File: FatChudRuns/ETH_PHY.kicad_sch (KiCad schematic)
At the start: 45 parts, among them U2 DP83848I

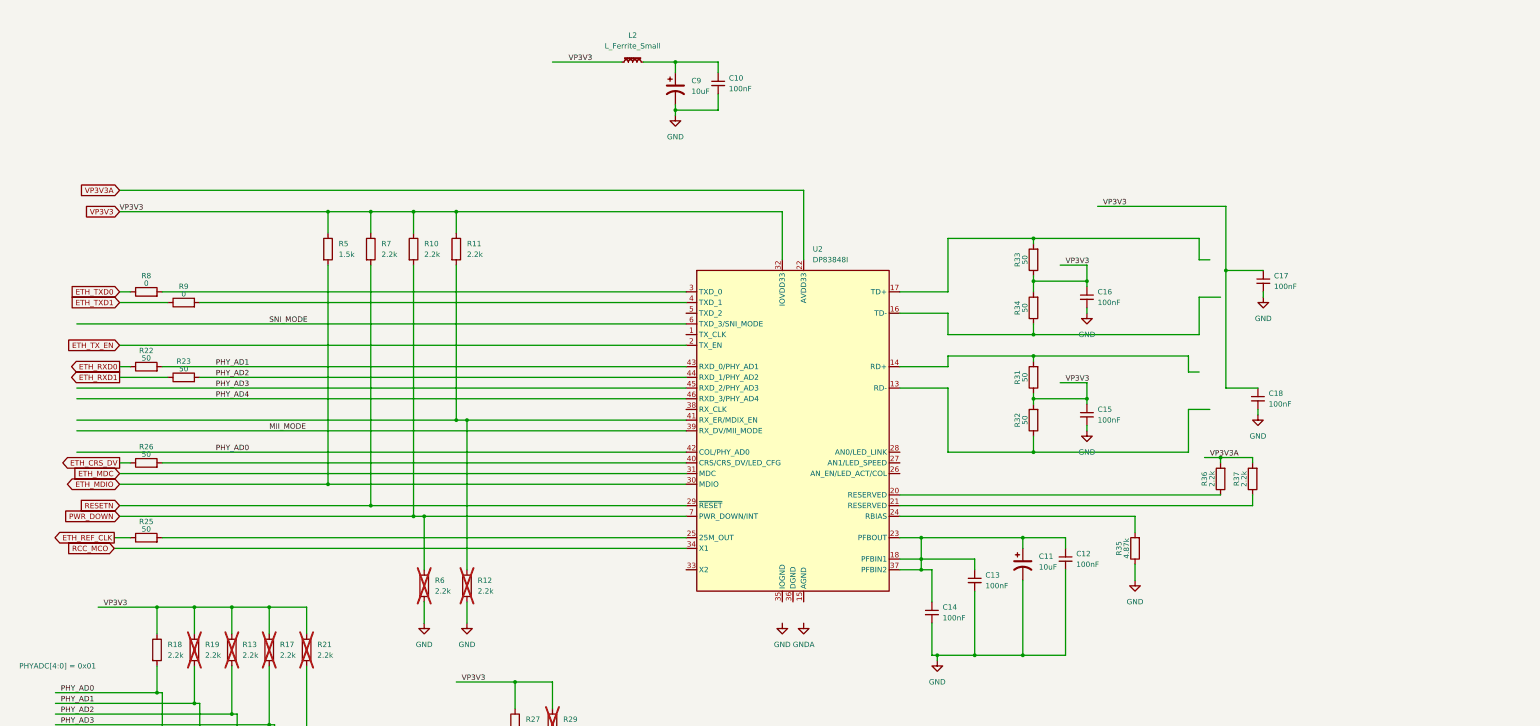
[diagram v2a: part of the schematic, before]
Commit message: selected rj45 w/ mag, fixed filtering for power, added snippets of layout recs
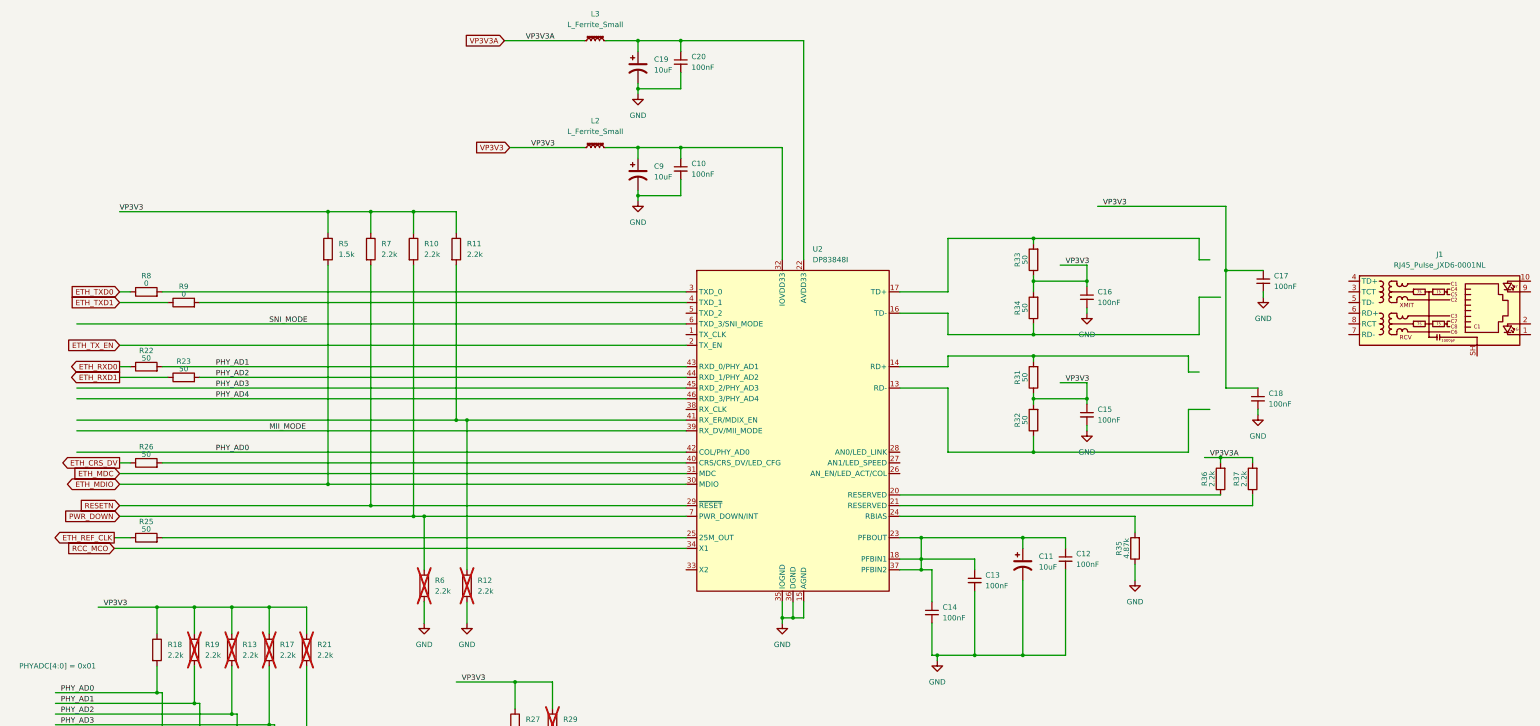
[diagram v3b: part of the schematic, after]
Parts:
- added C19: 10uF, symbol Device:C_Polarized_US
- added C20: 100nF, symbol Device:C_Small
- added J1: RJ45_Pulse_JXD6-0001NL, Connector_RJ:RJ45_Pulse_JXD6-0001NL_Horizontal, symbol Connector:RJ45_Pulse_JXD6-0001NL
- added L3: L_Ferrite_Small, symbol Device:L_Ferrite_Small
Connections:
- net GND: now also U2.15 (AGND), U2.19 (AGND), U2.35 (IOGND), U2.36 (DGND), U2.47 (IOGND), C19.2, C20.2
- net VP3V3: no longer U2.32 (IOVDD33), U2.48 (IOVDD33)
- net VP3V3A: now also L3.1; no longer U2.22 (AVDD33)
- net at C10.1, C9.1, L2.2: now also U2.32 (IOVDD33), U2.48 (IOVDD33)
- new net: C19.1, C20.1, L3.2, U2.22 (AVDD33)
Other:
- moved on the sheet: C10, C9, L2

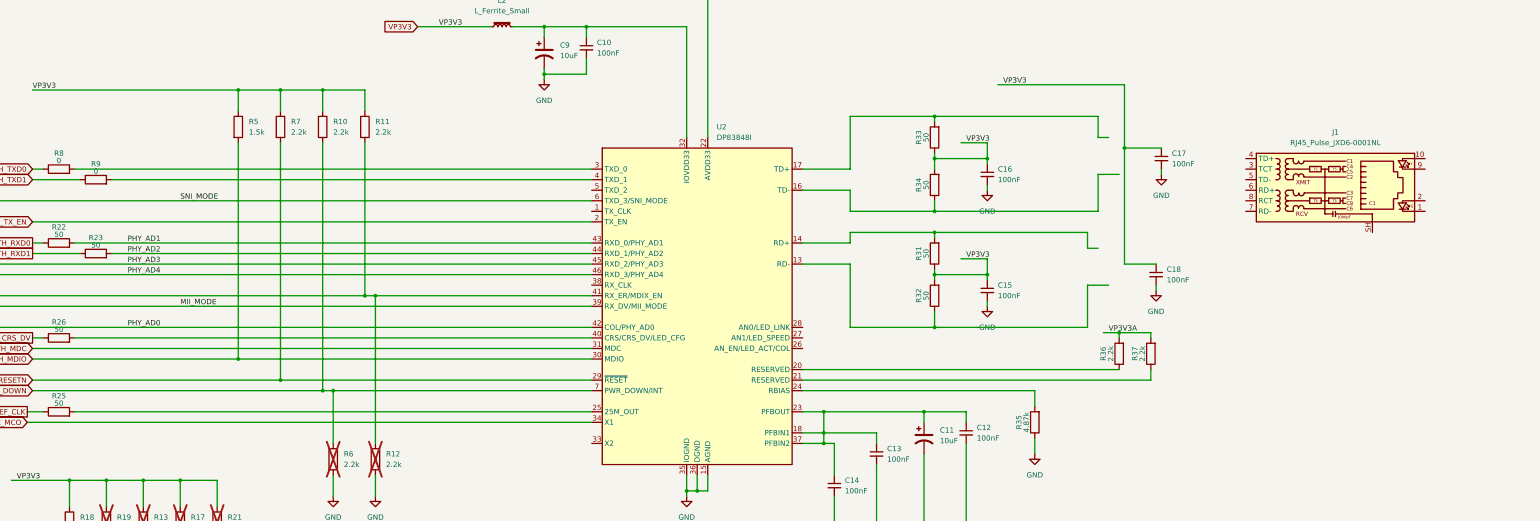
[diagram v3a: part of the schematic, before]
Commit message: connected rj45 and leds and led strapping resistors
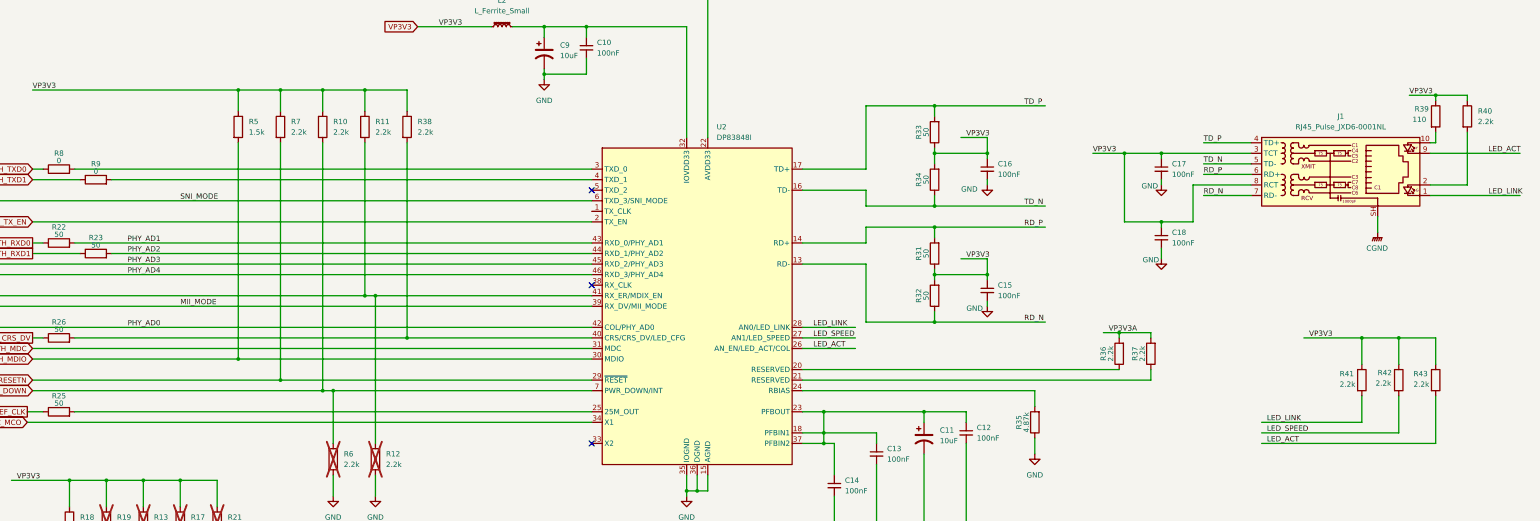
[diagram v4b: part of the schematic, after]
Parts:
- added R38, R40, R41, R42, R43: 2.2k, Resistor_SMD:R_0603_1608Metric, symbol Device:R
- added R39: 110, Resistor_SMD:R_0603_1608Metric, symbol Device:R
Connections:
- net VP3V3: now also J1.3 (TCT), J1.8 (RCT), R38.1, R39.1, R40.1, R41.1, R42.1, R43.1
- net RD_P: now reaches R31.2, U2.14 (RD+)
- net RD_P: now also J1.6 (RD+)
- net TD_P: now reaches R33.2, U2.17 (TD+)
- net TD_P: now also J1.4 (TD+)
- net TD_N: now reaches R34.1, U2.16 (TD-)
- net TD_N: now also J1.5 (TD-)
- net RD_N: now reaches R32.1, U2.13 (RD-)
- net RD_N: now also J1.7 (RD-)
- net LED_ACT: now reaches U2.26 (AN_EN/LED_ACT/COL)
- net LED_ACT: now also J1.9, R43.2
- net LED_SPEED: now reaches U2.27 (AN1/LED_SPEED)
- net LED_SPEED: now also R42.2
- net LED_LINK: now reaches U2.28 (AN0/LED_LINK)
- net LED_LINK: now also J1.1, R41.2
- net at R26.2, U2.40 (CRS/CRS_DV/LED_CFG): now also R38.2
- net at J1.10: now also R39.2
- net at J1.2: now also R40.2
- net CGND: now reaches J1.SH
- no-connect marks 0 -> 3
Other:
- moved on the sheet: C16, C17, C18, J1, R33, R34

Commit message: connected remaining gpio pins to connector, added kicad power pins instead of net names
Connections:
- net VP3V3 renamed +3.3V
- net VP3V3A renamed +3.3VA

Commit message: add usb c power circuitry, added led for power indication, increased resistance of ethernet leds light to 220ohms
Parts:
- removed L2, L3: L_Ferrite_Small, symbol Device:L_Ferrite_Small
- added R45, R46: 0, Resistor_SMD:R_0603_1608Metric, symbol Device:R
- R39: value 110 -> 220
- R40: value 2.2k -> 220
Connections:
- net +3.3V: now also R45.1
- net +3.3VA: now also R46.1
- net at C10.1, C9.1, U2.32 (IOVDD33)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: now also R45.2
- net at C19.1, C20.1, U2.22 (AVDD33): now also R46.2

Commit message: sorted out erc errors and warning, connected tvs diodes to jtag
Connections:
- net MDIX_EN: now reaches R11.2, R12.1, U2.41 (RX_ER/MDIX_EN)
- no-connect marks 3 -> 4

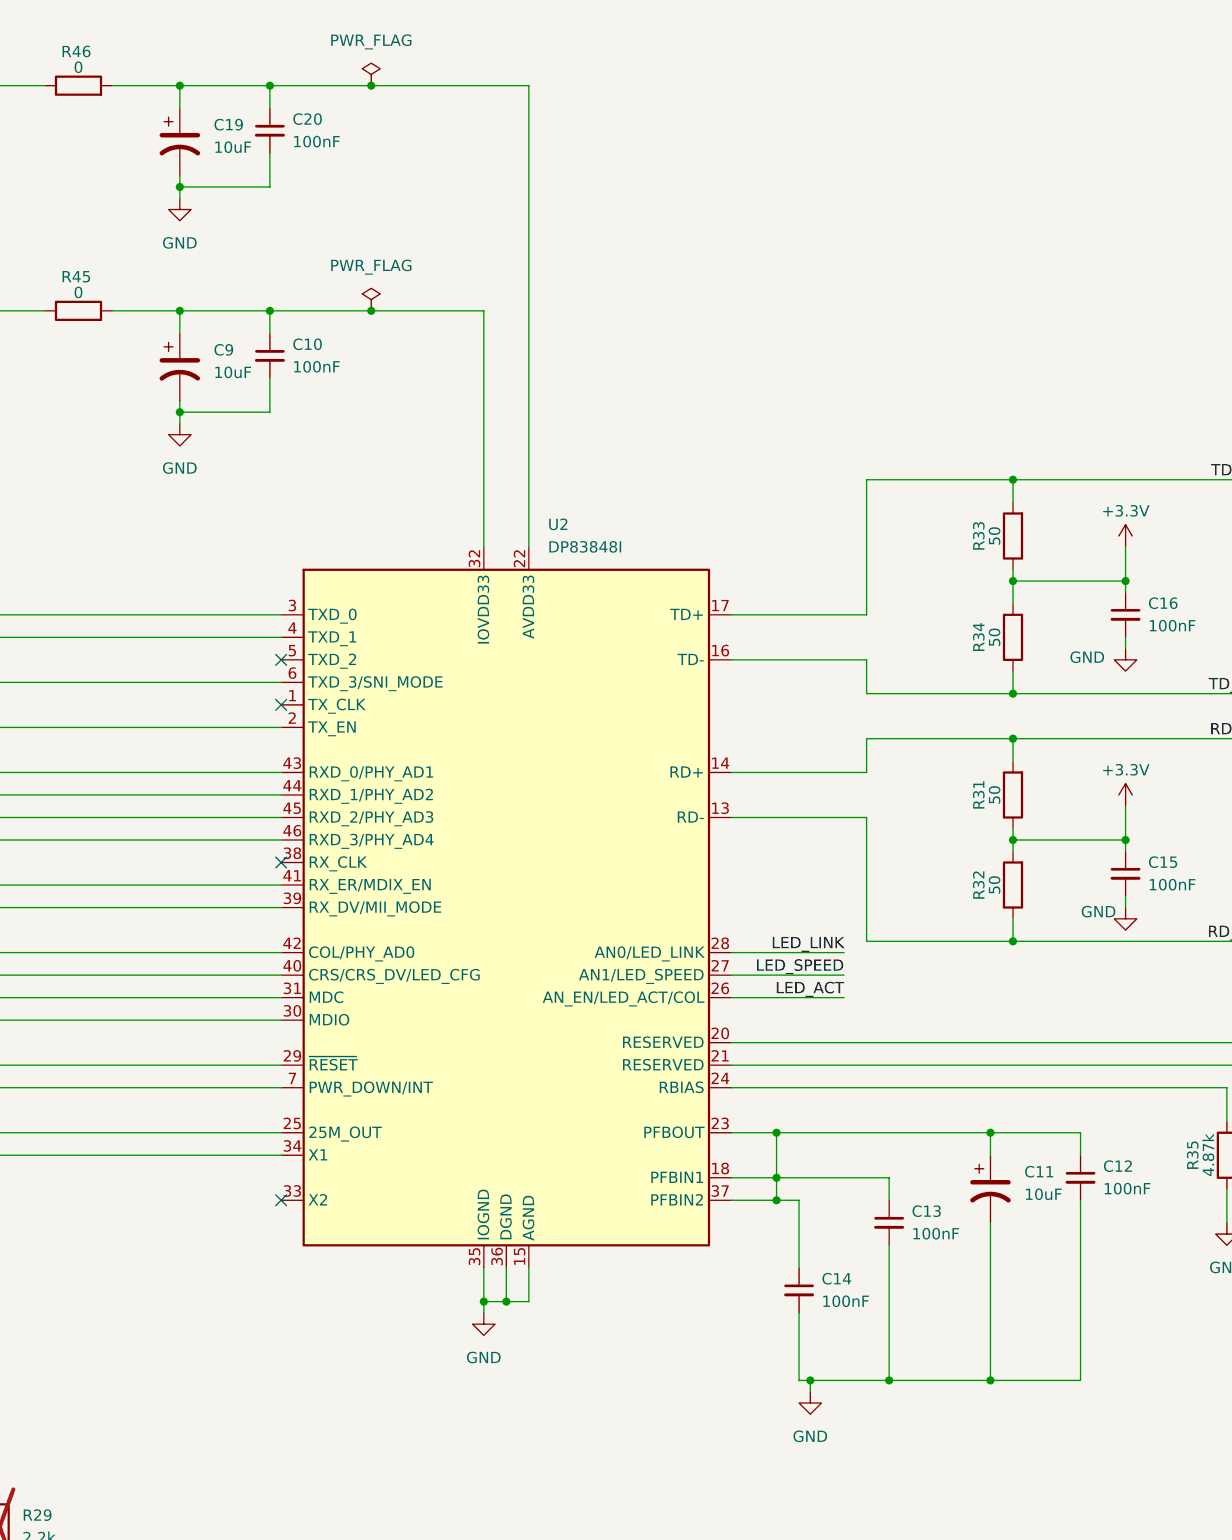
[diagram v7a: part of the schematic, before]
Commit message: added caps and diode footprints, all caps now non-polarized ceramic caps
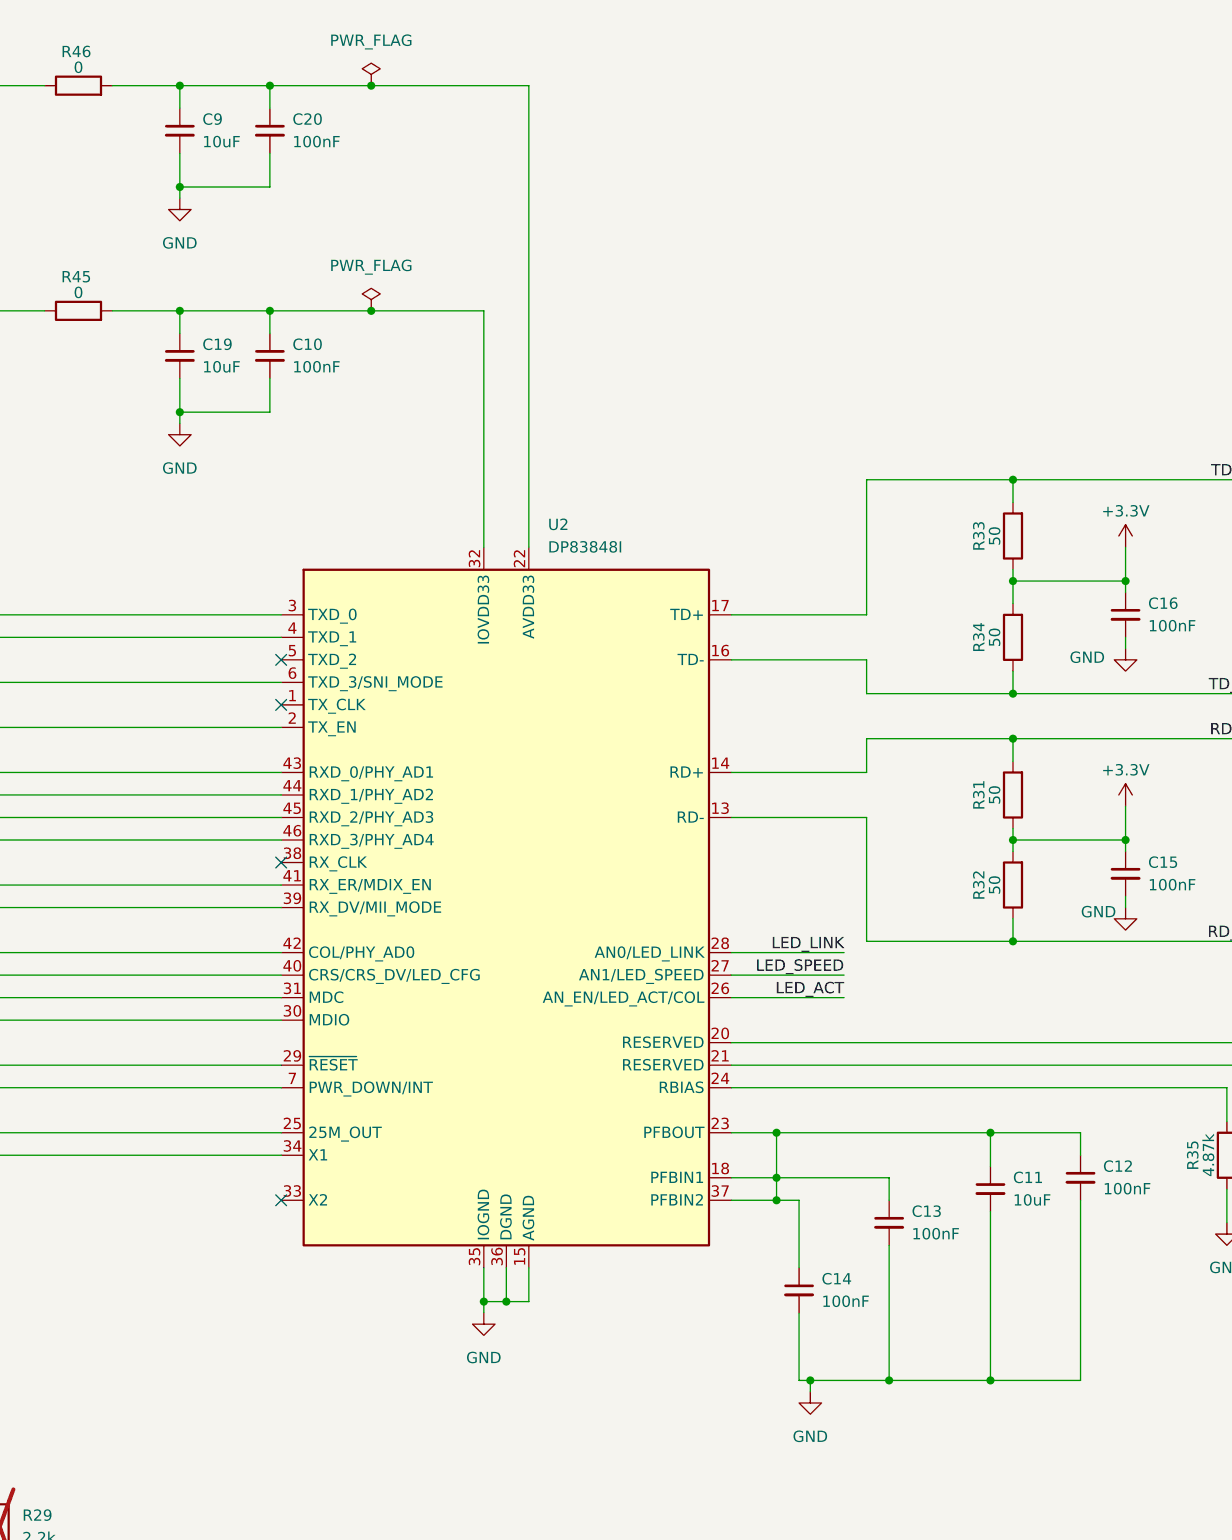
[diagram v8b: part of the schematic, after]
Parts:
- removed C11, C19, C9: 10uF, symbol Device:C_Polarized_US
- added C11, C19, C9: 10uF, Capacitor_SMD:C_0603_1608Metric, symbol Device:C_Small
- C10, C12, C13, C14, C15, C16, C17, C18, C20: footprint (none) -> Capacitor_SMD:C_0603_1608Metric
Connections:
- net GND: now also C11.2, C19.2, C9.2
- net at C10.1, R45.2, U2.32 (IOVDD33)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: now also C19.1
- net at C12.1, C13.1, C14.1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: now also C11.1
- net at C20.1, R46.2, U2.22 (AVDD33): now also C9.1
